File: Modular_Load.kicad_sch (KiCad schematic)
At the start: 57 parts, among them J2 Conn_01x04_Male, J3 7466203, J4 Conn_01x02_Male, J5 7466203, Q2 IGT65R025D2, U1 ADA4807-4

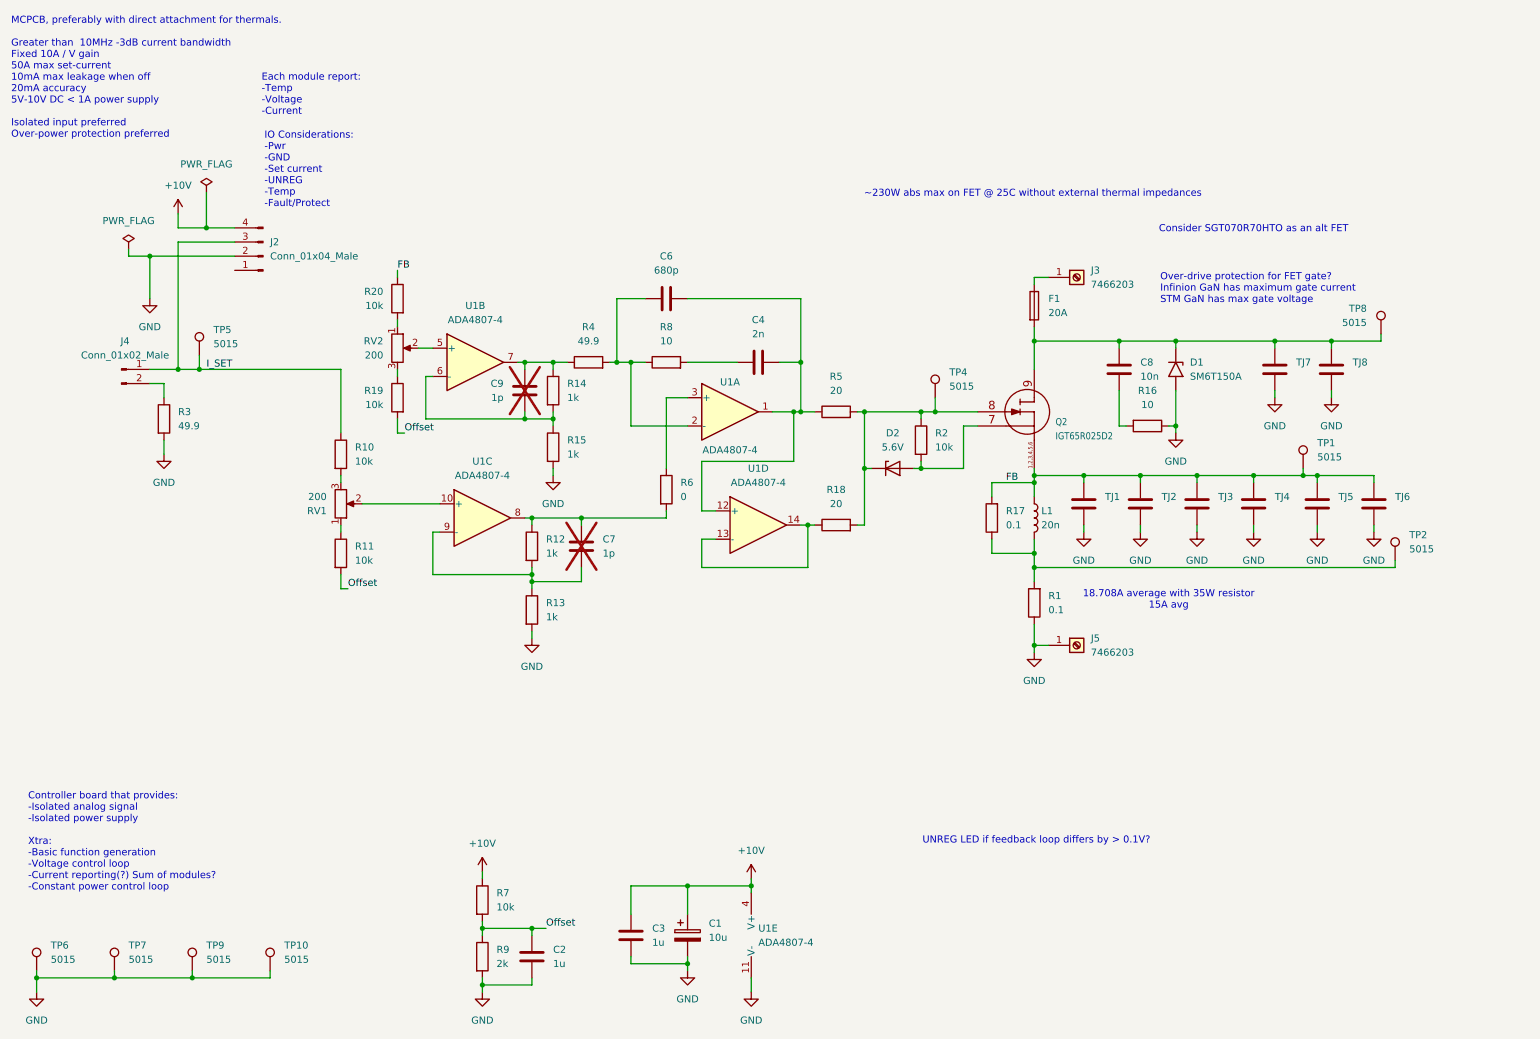
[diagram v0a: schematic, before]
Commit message: Add files via upload
V2, added MMCX connectors, adjusted gain tuning, changed control connector, thermal layout update.
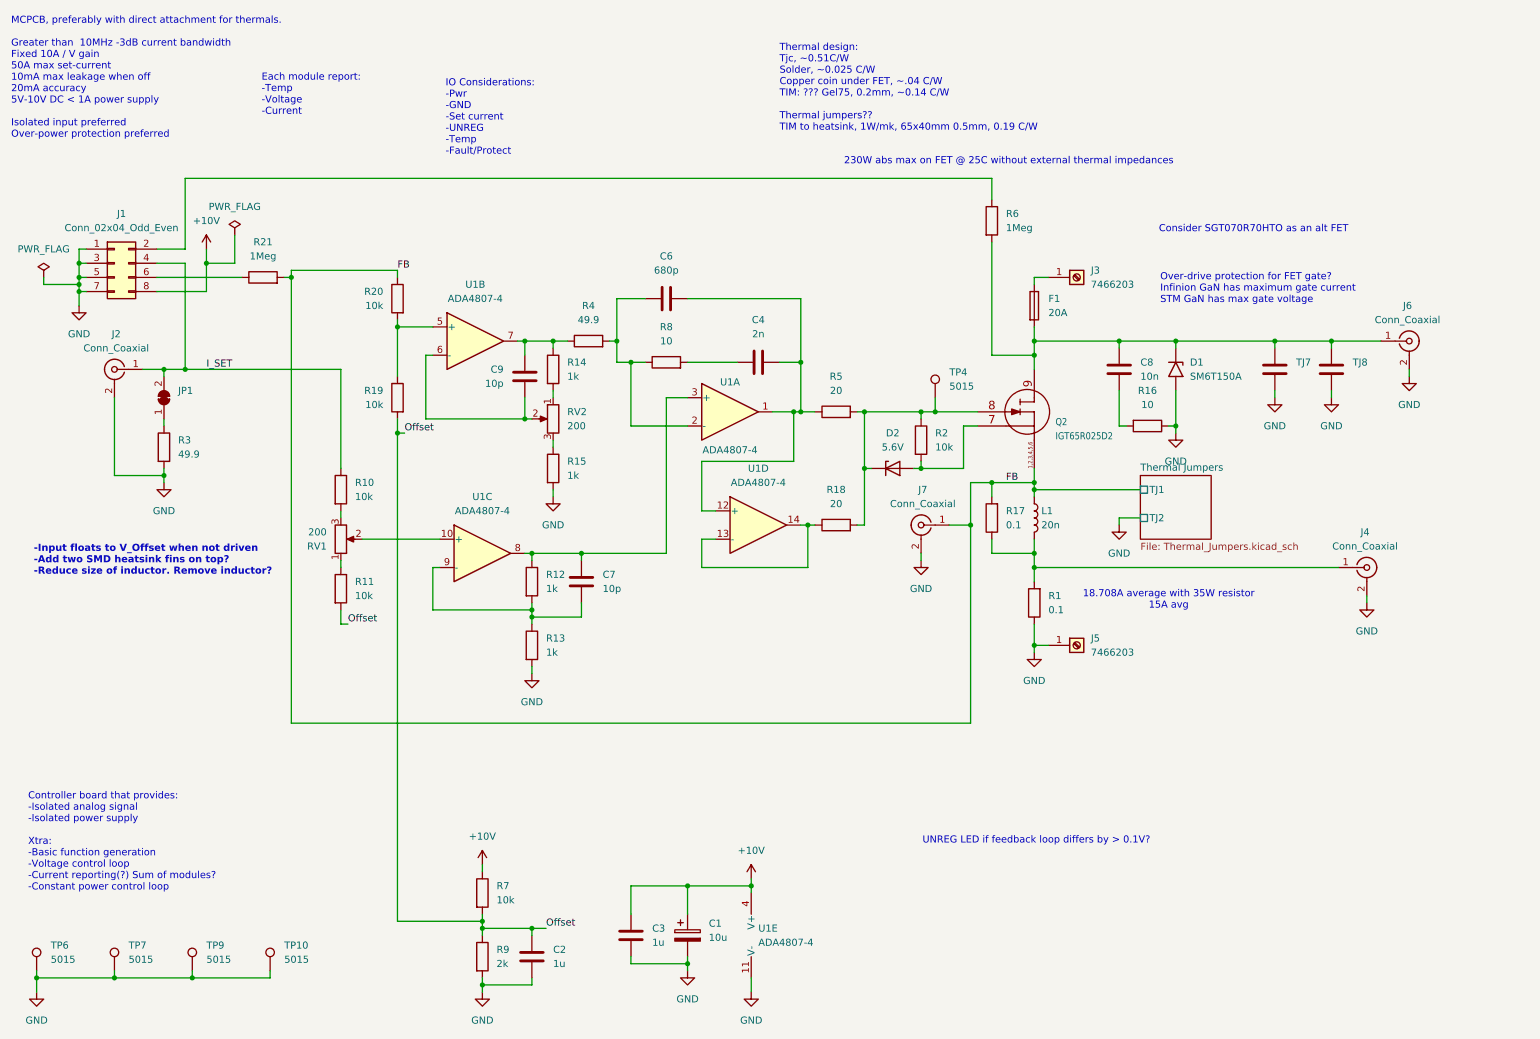
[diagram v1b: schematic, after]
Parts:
- removed J2: Conn_01x04_Male, Connector_PinHeader_2.54mm:PinHeader_1x04_P2.54mm_Vertical_SMD_Pin1Left, symbol Connector:Conn_01x04_Male
- removed J4: Conn_01x02_Male, Connector_PinHeader_2.54mm:PinHeader_1x02_P2.54mm_Vertical_SMD_Pin1Left, symbol Connector:Conn_01x02_Male
- removed TJ1, TJ2, TJ3, TJ4, TJ5, TJ6: THJP0612ABT1, Resistor_SMD:R_0612_1632Metric_Pad1.18x3.40mm_HandSolder, symbol Device:C
- removed TP1, TP2, TP5, TP8: 5015, TestPoint:TestPoint_Keystone_5015_Micro_Mini, symbol Connector:TestPoint
- added J1: Conn_02x04_Odd_Even, Connector_PinHeader_2.54mm:PinHeader_2x04_P2.54mm_Vertical_SMD, symbol Connector_Generic:Conn_02x04_Odd_Even
- added J2, J4, J6, J7: Conn_Coaxial, Connector_Coaxial:WR-MMCX_Wuerth_66012102111404_Vertical, symbol Connector:Conn_Coaxial
- added JP1: SolderJumper_2_Bridged, Jumper:SolderJumper-2_P1.3mm_Bridged_RoundedPad1.0x1.5mm, symbol Jumper:SolderJumper_2_Bridged
- added R21: 1Meg, Resistor_SMD:R_0603_1608Metric, symbol Device:R
- C7, C9: value 1p -> 10p; now fitted
- C8: footprint Capacitor_SMD:C_0603_1608Metric -> Capacitor_SMD:C_1206_3216Metric
- R6: value 0 -> 1Meg; PartNumber CRCW06030000Z0EA -> (none)
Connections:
- net +10V: now also J1.8 (Pin_8)
- net FB: now also J7.1 (In), R21.2
- net GND: now also J1.1 (Pin_1), J1.3 (Pin_3), J1.5 (Pin_5), J1.7 (Pin_7), J2.2 (Ext), J4.2 (Ext), J6.2 (Ext), J7.2 (Ext)
- net I_SET: now also J1.4 (Pin_4), J2.1 (In), JP1.2 (B)
- net at U1.3 (+): now also C7.1, R12.1, U1.8; no longer R6.1
- net at C8.1, D1.1 (A1), F1.2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: now also R6.2, J6.1 (In)
- net at C9.2, U1.6 (-): now also RV2.2; no longer R14.2, R15.1
- net at L1.2, R1.2, R17.1: now also J4.1 (In)
- net at RV2.1: now also R14.2; no longer R20.2
- net at U1.5 (+): now also R19.1, R20.2; no longer RV2.2
- net at RV2.3: now also R15.1; no longer R19.1
- net at R3.1: now also JP1.1 (A)
- new net: J1.2 (Pin_2), R6.1
- new net: J1.6 (Pin_6), R21.1
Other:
- added sheet Thermal Jumpers (Thermal_Jumpers.kicad_sch)
- note added: "-Input floats to V_Offset when not driven -Add two SMD heatsink fins on top? -Reduce size of inductor. Remove inductor?"
- note added: "230W abs max on FET @ 25C without external thermal impedances"
- note added: "Thermal design: Tjc, ~0.51C/W Solder, ~0.025 C/W Copper coin under FET, ~.04 C/W TIM: ??? Gel75, 0.2mm, ~0.14 C/W Thermal jumpers?? TIM to heatsink, 1W/mk, 65x40mm 0.5mm, 0.19 C/W"
- note removed: "~230W abs max on FET @ 25C without external thermal impedances"
- moved on the sheet: R10, R11, R12, R13, R14, R15, R3, R4, R7, RV1, RV2, U1B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

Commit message: V3 Update
Thermal improvements, double-sided assembly, better reference stability
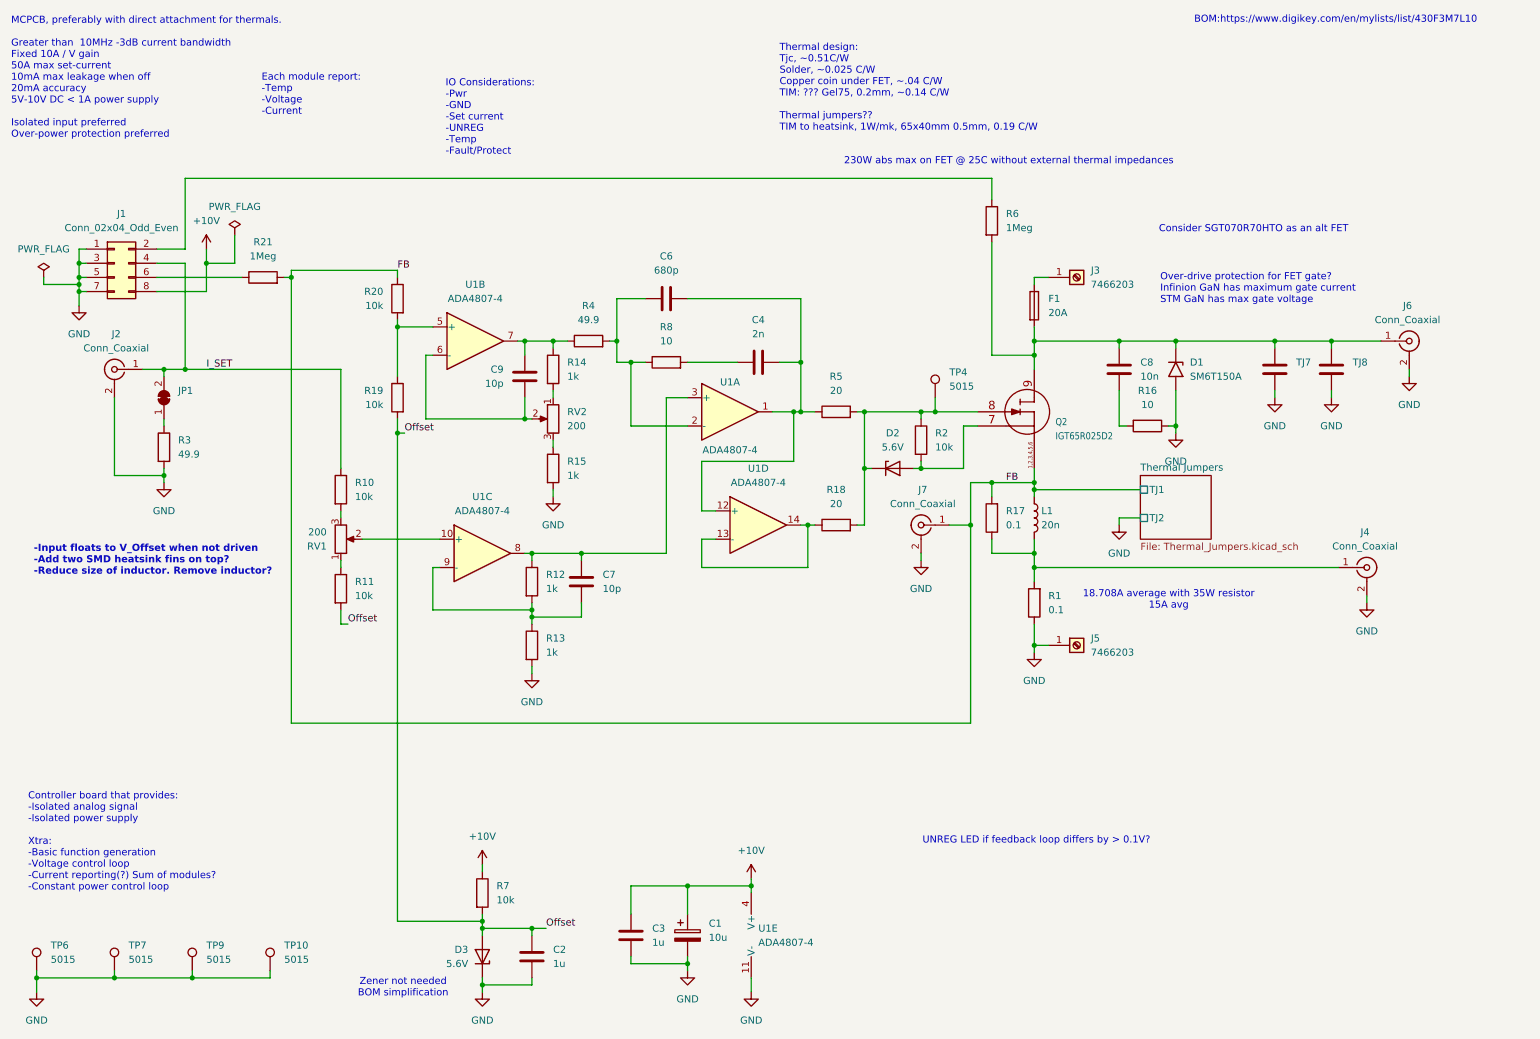
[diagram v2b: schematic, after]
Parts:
- removed R9: 2k, Resistor_SMD:R_0603_1608Metric, symbol Device:R
- added D3: 5.6V, Diode_SMD:D_SOD-323_HandSoldering, symbol Device:D_Zener
- C7, C9: PartNumber (none) -> C0603C100J5GACTU
- R21, R6: PartNumber (none) -> CRCW06031M00FKEA
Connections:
- net GND: now also D3.1 (K)
- net Offset: now also D3.2 (A)
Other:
- note added: "BOM:https://www.digikey.com/en/mylists/list/430F3M7L10"
- note added: "Zener not needed BOM simplification"
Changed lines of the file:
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@@
 	(generator_version "9.0")
 	(paper "A4")
+	(text "BOM:https://www.digikey.com/en/mylists/list/430F3M7L10"
+		(exclude_from_sim no)
+		(at 252.222 16.002 0)
+		(effects
+			(font
+				(size 1.27 1.27)
+			)
+		)
+	)
 	(text "Thermal design:\nTjc, ~0.51C/W\nSolder, ~0.025 C/W\nCopper coin under FET, ~.04 C/W\nTIM: ??? Gel75, 0.2mm, ~0.14 C/W\n\nThermal jumpers??\nTIM to heatsink, 1W/mk, 65x40mm 0.5mm, 0.19 C/W"
 		(exclude_from_sim no)
@@
 		)
 	)
+	(text "Zener not needed\nBOM simplification"
+		(exclude_from_sim no)
+		(at 84.836 189.738 0)
+		(effects
+			(font
+				(size 1.27 1.27)
+			)
+		)
+	)
 	(text "UNREG LED if feedback loop differs by > 0.1V?"
 		(exclude_from_sim no)
@@
 			)
 		)
+		(property "PartNumber" "CRCW06031M00FKEA"
+			(at 190.5 52.07 0)
+			(effects
+				(font
+					(size 1.27 1.27)
+				)
+				(hide yes)
+			)
+		)
 		(pin "1"
 		)
@@
 			)
 		)
+		(property "PartNumber" "C0603C100J5GACTU"
+			(at 106.68 80.01 0)
+			(effects
+				(font
+					(size 1.27 1.27)
+				)
+				(hide yes)
+			)
+		)
 		(pin "2"
 		)
@@
 	)
 	(symbol
+		(lib_id "Device:D_Zener")
+		(at 99.06 184.15 270)
+		(mirror x)
+		(unit 1)
+		(exclude_from_sim no)
+		(in_bom yes)
+		(on_board yes)
+		(dnp no)
+		(property "Reference" "D3"
+			(at 96.52 182.8799 90)
+			(effects
+				(font
+					(size 1.27 1.27)
+				)
+				(justify right)
+			)
+		)
+		(property "Value" "5.6V"
+			(at 96.52 185.4199 90)
+			(effects
+				(font
+					(size 1.27 1.27)
+				)
+				(justify right)
+			)
+		)
+		(property "Footprint" "Diode_SMD:D_SOD-323_HandSoldering"
+			(at 99.06 184.15 0)
+			(effects
+				(font
+					(size 1.27 1.27)
+				)
+				(hide yes)
+			)
+		)
+		(property "Datasheet" "https://www.diodes.com/assets/Datasheets/ds31987.pdf"
+			(at 99.06 184.15 0)
+			(effects
+				(font
+					(size 1.27 1.27)
+				)
+				(hide yes)
+			)
+		)
+		(property "Description" "Zener diode"
+			(at 99.06 184.15 0)
+			(effects
+				(font
+					(size 1.27 1.27)
+				)
+				(hide yes)
+			)
+		)
+		(property "PartNumber" "DDZ5V6BSF-7"
+			(at 99.06 184.15 0)
+			(effects
+				(font
+					(size 1.27 1.27)
+				)
+				(hide yes)
+			)
+		)
+		(pin "1"
+		)
+		(pin "2"
+		)
+		(instances
+			(project "Modular_Load"
+				(path "/b7c09c15-282b-4731-8942-008851172201"
+					(reference "D3")
+					(unit 1)
+				)
+			)
+		)
+	)
+	(symbol
 		(lib_id "Device:R_Potentiometer")
 		(at 73.66 109.22 0)
@@
 			)
 		)
+		(property "PartNumber" "C0603C100J5GACTU"
+			(at 116.84 116.84 0)
+			(effects
+				(font
+					(size 1.27 1.27)
+				)
+				(hide yes)
+			)
+		)
 		(pin "2"
 		)
@@
 			)
 		)
+		(property "PartNumber" "CRCW06031M00FKEA"
+			(at 59.69 62.23 90)
+			(effects
+				(font
+					(size 1.27 1.27)
+				)
+				(hide yes)
+			)
+		)
 		(pin "1"
 		)
@@
 					(unit 1)
 				)
-			)
-		)
-	)
-	(symbol
-		(lib_id "Device:R")
-		(at 99.06 184.15 0)
-		(unit 1)
-		(exclude_from_sim no)
-		(in_bom yes)
-		(on_board yes)
-		(dnp no)
-		(fields_autoplaced yes)
-		(property "Reference" "R9"
-			(at 101.6 182.8799 0)
-			(effects
-				(font
-					(size 1.27 1.27)
-				)
-				(justify left)
-			)
-		)
-		(property "Value" "2k"
-			(at 101.6 185.4199 0)
-			(effects
-				(font
-					(size 1.27 1.27)
-				)
-				(justify left)
-			)
-		)
-		(property "Footprint" "Resistor_SMD:R_0603_1608Metric"
-			(at 97.282 184.15 90)
-			(effects
-				(font
-					(size 1.27 1.27)
-				)
-				(hide yes)
-			)
-		)
-		(property "Datasheet" "https://www.vishay.com/docs/20035/dcrcwe3.pdf"
-			(at 99.06 184.15 0)
-			(effects
-				(font
-					(size 1.27 1.27)
-				)
-				(hide yes)
-			)
-		)
-		(property "Description" "Resistor"
-			(at 99.06 184.15 0)
-			(effects
-				(font
-					(size 1.27 1.27)
-				)
-				(hide yes)
-			)
-		)
-		(property "Mates with" ""
-			(at 99.06 184.15 0)
-			(effects
-				(font
-					(size 1.27 1.27)
-				)
-				(hide yes)
-			)
-		)
-		(property "PartNumber" "CRCW06032K00FKEA"
-			(at 99.06 184.15 0)
-			(effects
-				(font
-					(size 1.27 1.27)
-				)
-				(hide yes)
-			)
-		)
-		(pin "2"
-		)
-		(pin "1"
-		)
-		(instances
-			(project ""
-				(path "/b7c09c15-282b-4731-8942-008851172201"
-					(reference "R9")
-					(unit 1)
-				)
